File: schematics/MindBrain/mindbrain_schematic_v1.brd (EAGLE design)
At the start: 100 x 80 mm, 47 parts, among them CON1 POWER, IC1 TL084P, IC2 TL084P

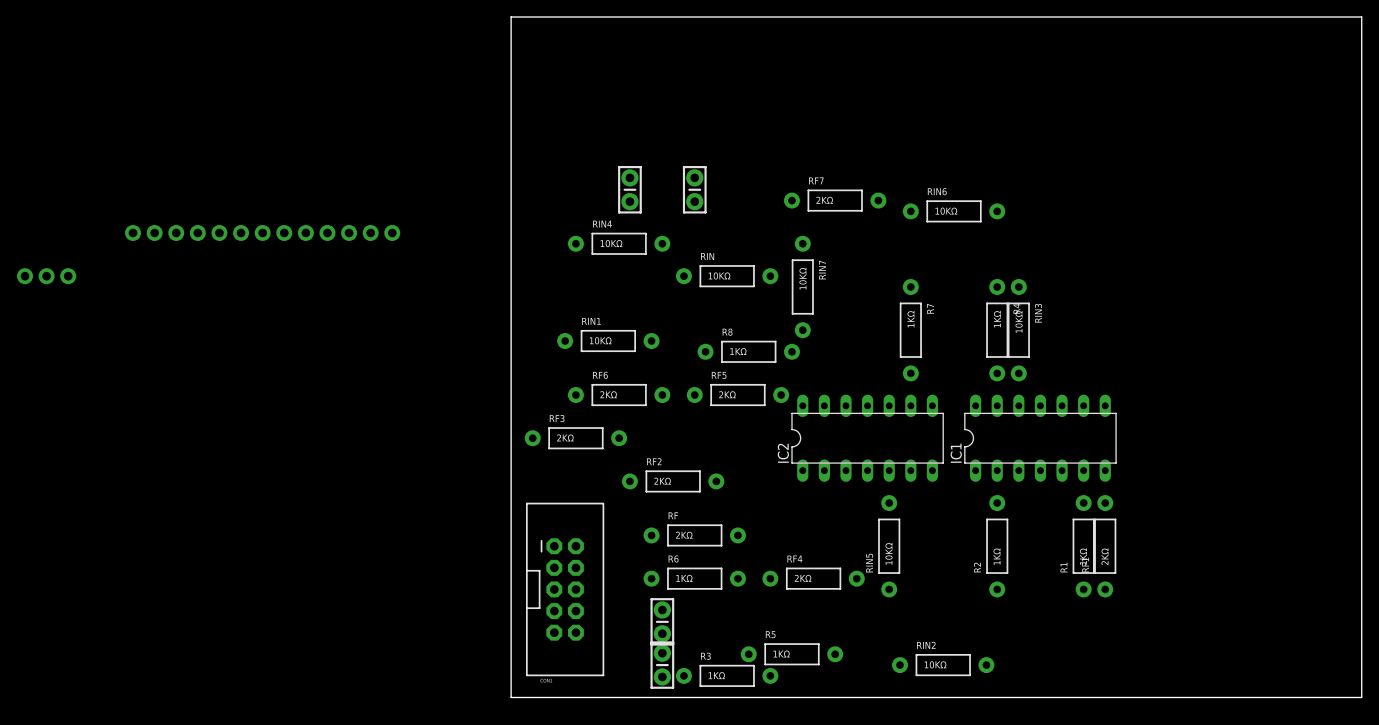
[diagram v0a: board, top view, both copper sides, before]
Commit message: fixed component designator confusion
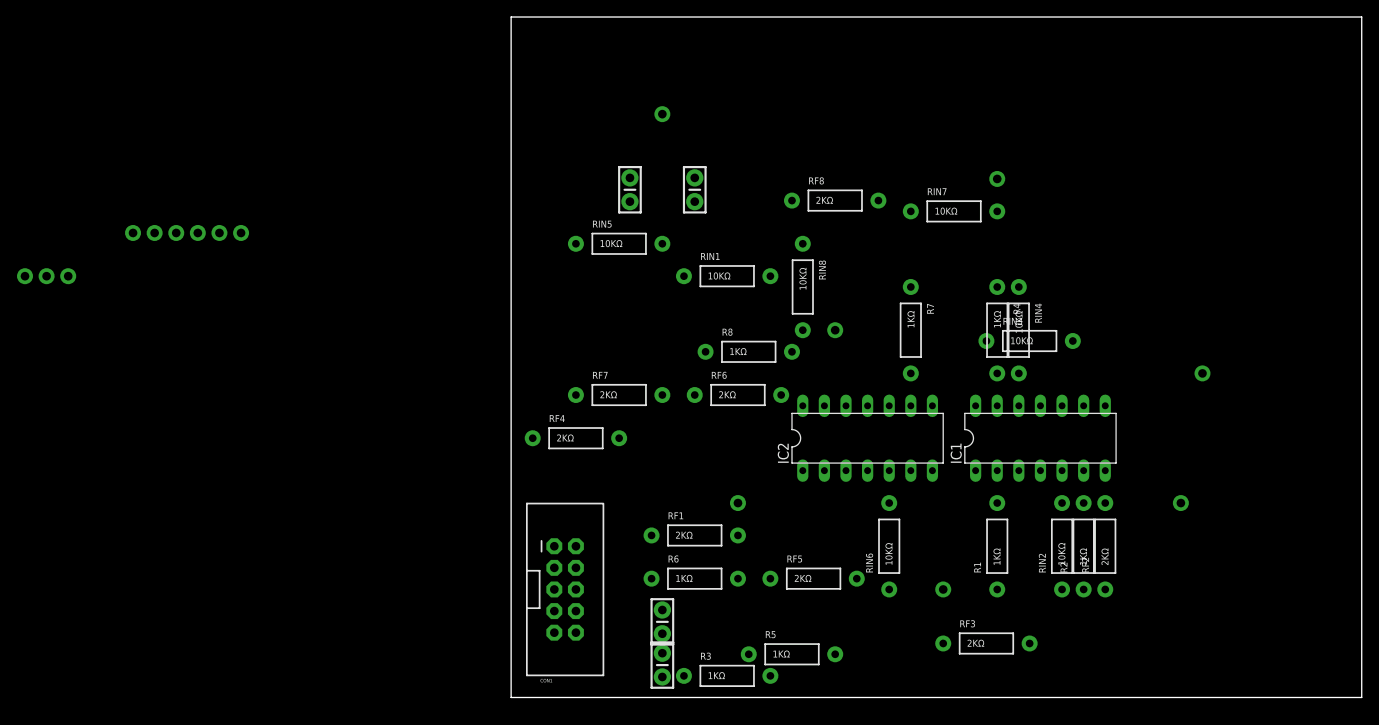
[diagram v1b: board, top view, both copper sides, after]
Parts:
- removed RF: 2KΩ, SparkFun-Passives:AXIAL-0.4
- removed RIN: 10KΩ, SparkFun-Passives:AXIAL-0.4
- added RF8: 2KΩ, SparkFun-Passives:AXIAL-0.4
- added RIN8: 10KΩ, SparkFun-Passives:AXIAL-0.4
- moved OUTPUT2 112.5 mm to (78.7, 22.9)
- moved INPUT4 96.7 mm to (81.3, 38.1)
- moved INPUT6 81.5 mm to (50.8, 12.7)
- moved INPUT7 79.0 mm to (57.1, 61.0)
- moved INPUT8 63.3 mm to (38.1, 43.2)
- moved OUTPUT1 62.1 mm to (26.7, 22.9)
- moved RF3 54.0 mm to (55.9, 6.35)
- moved RF2 51.4 mm to (69.8, 17.8), turned to 90 degrees
- moved RF1 48.3 mm to (21.6, 19.1), turned to 0 degrees
- moved RIN4 48.1 mm to (59.7, 43.2), turned to 270 degrees
- moved RIN5 47.7 mm to (12.7, 53.3), turned to 0 degrees
- moved RIN6 40.1 mm to (44.5, 17.8), turned to 90 degrees
- moved INPUT5 37.0 mm to (17.8, 68.6)
- moved RF7 34.2 mm to (12.7, 35.6)
- moved RF4 32.5 mm to (7.62, 30.5)
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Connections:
- net GND: now also RIN8.P$1; no longer RIN.P$1
- net N$1: now also RIN1.P$2; no longer RIN.P$2
- net N$10: now also RIN4.P$2; no longer RIN3.P$2
- net N$11: now also RF4.P$2; no longer RF3.P$2
- net N$12: now also RF4.P$1; no longer RF3.P$1
- net N$13: now also RIN5.P$2; no longer RIN4.P$2
- net N$14: now also RF5.P$2; no longer RF4.P$2
- net N$15: now also RF5.P$1; no longer RF4.P$1
- net N$16: now also RIN6.P$2; no longer RIN5.P$2
- net N$17: now also RF6.P$2; no longer RF5.P$2
- net N$18: now also RF6.P$1; no longer RF5.P$1
- net N$19: now also RIN7.P$2; no longer RIN6.P$2
- net N$2: now also RF1.P$2; no longer RF.P$2
- net N$20: now also RF7.P$2; no longer RF6.P$2
- net N$21: now also RF7.P$1; no longer RF6.P$1
- net N$22: now also RIN8.P$2; no longer RIN7.P$2
- net N$23: now also RF8.P$2; no longer RF7.P$2
- net N$24: now also RF8.P$1; no longer RF7.P$1
- net N$3: now also R1.P$2, RF1.P$1; no longer R2.P$2, RF.P$1
- net N$4: now also RIN2.P$2; no longer RIN1.P$2
- net N$5: now also RF2.P$2; no longer RF1.P$2
- net N$6: now also R2.P$2, RF2.P$1; no longer R1.P$2, RF1.P$1
- net N$7: now also RIN3.P$2; no longer RIN2.P$2
- net N$8: now also RF3.P$2; no longer RF2.P$2
- net N$9: now also RF3.P$1; no longer RF2.P$1

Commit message: completed basic board placement
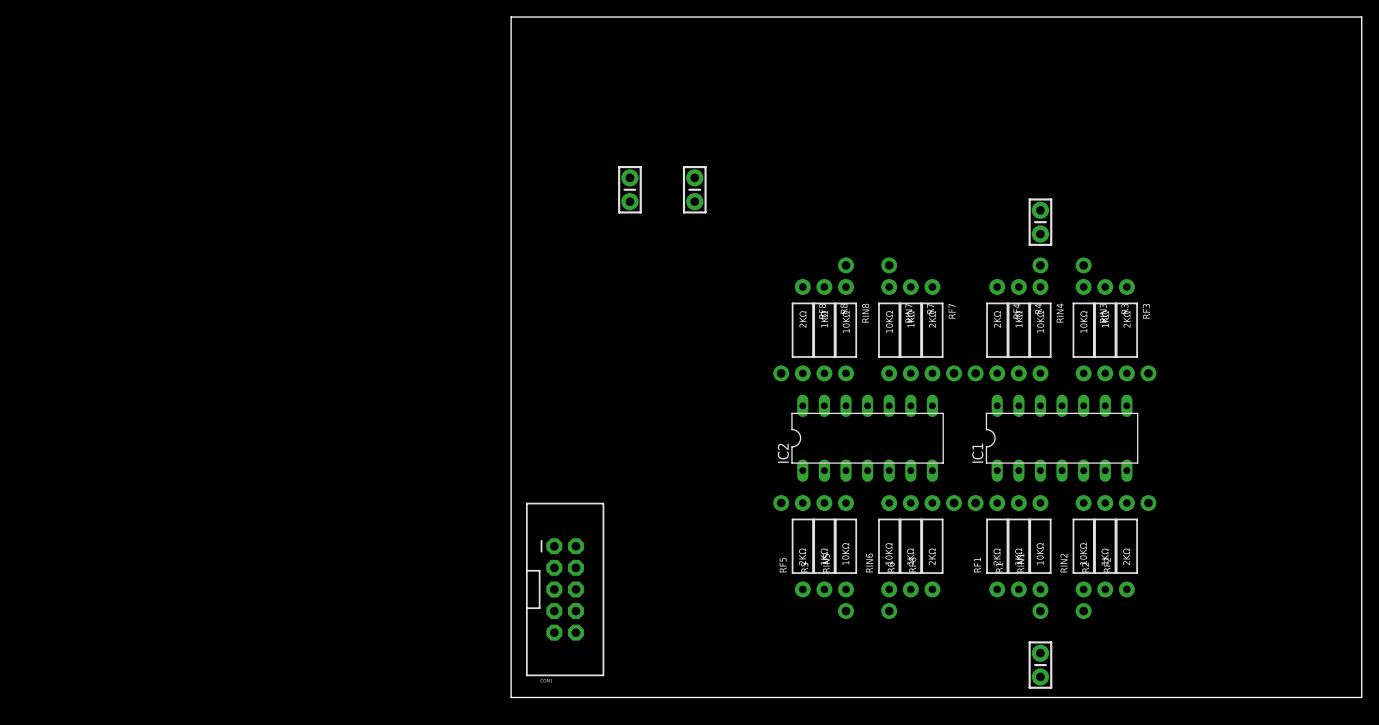
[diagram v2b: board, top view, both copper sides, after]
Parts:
- moved INPUT2 128.1 mm to (67.3, 10.2)
- moved INPUT3 124.5 mm to (67.3, 50.8)
- moved INPUT1 120.9 mm to (62.2, 10.2)
- moved OUTPUT3 108.0 mm to (74.9, 38.1)
- moved OUTPUT6 96.8 mm to (52.1, 22.9)
- moved OUTPUT7 95.4 mm to (52.1, 38.1)
- moved OUTPUT4 90.4 mm to (54.6, 38.1)
- moved OUTPUT8 78.0 mm to (31.8, 38.1)
- moved OUTPUT5 75.6 mm to (31.8, 22.9)
- moved C3 68.5 mm to (62.2, 55.9)
- moved INPUT5 62.3 mm to (39.4, 10.2)
- moved R3 60.2 mm to (69.8, 43.2), turned to 270 degrees
- moved RF4 51.1 mm to (57.1, 43.2), turned to 270 degrees
- moved RIN1 48.6 mm to (62.2, 17.8), turned to 90 degrees
- moved C2 44.7 mm to (62.2, 3.81)
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
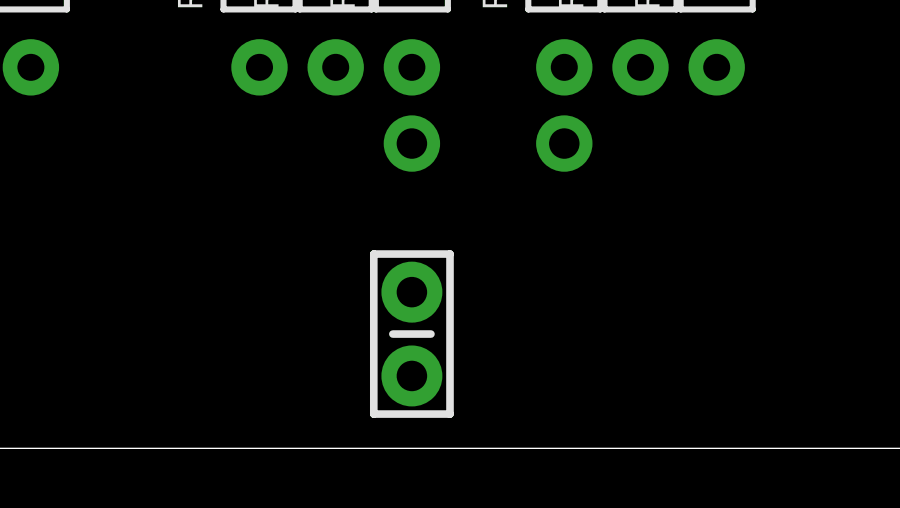
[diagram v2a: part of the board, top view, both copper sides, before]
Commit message: connected power supply grounds to circuit ground
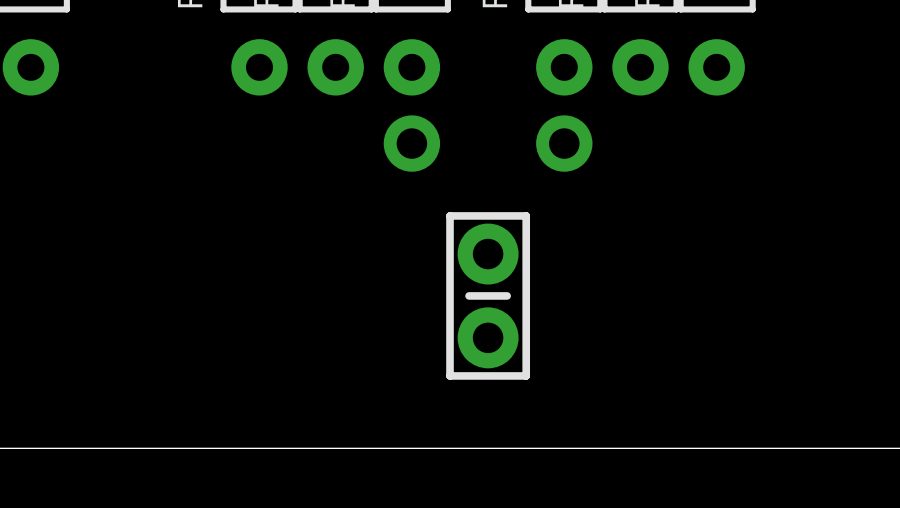
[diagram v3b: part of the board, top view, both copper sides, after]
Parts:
- moved C2 2.84 mm to (64.8, 5.08)
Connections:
- removed net N$25: CON1.3, CON1.4, CON1.5, CON1.6, CON1.7, CON1.8
- net GND: now also CON1.3, CON1.4, CON1.5, CON1.6, CON1.7, CON1.8
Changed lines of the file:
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@@
 <element name="RIN8" library="SparkFun-Passives" package="AXIAL-0.4" value="10KΩ" x="39.37" y="43.18" rot="R270"/>
 <element name="C1" library="SparkFun-Capacitors" package="CAP-PTH-SMALL-KIT" value="" x="13.97" y="59.69" rot="R90"/>
-<element name="C2" library="SparkFun-Capacitors" package="CAP-PTH-SMALL-KIT" value="" x="62.23" y="3.81" rot="R90"/>
+<element name="C2" library="SparkFun-Capacitors" package="CAP-PTH-SMALL-KIT" value="" x="64.77" y="5.08" rot="R90"/>
 <element name="C3" library="SparkFun-Capacitors" package="CAP-PTH-SMALL-KIT" value="" x="62.23" y="55.88" rot="R90"/>
 <element name="C4" library="SparkFun-Capacitors" package="CAP-PTH-SMALL-KIT" value="" x="21.59" y="59.69" rot="R90"/>
@@
 <contactref element="RIN8" pad="P$1"/>
 <contactref element="R8" pad="P$1"/>
-<wire x1="46.99" y1="12.7" x2="69.85" y2="48.26" width="0" layer="19" extent="1-1"/>
-<wire x1="59.69" y1="12.7" x2="69.85" y2="48.26" width="0" layer="19" extent="1-1"/>
-<wire x1="36.83" y1="12.7" x2="59.69" y2="12.7" width="0" layer="19" extent="1-1"/>
-<wire x1="36.83" y1="48.26" x2="36.83" y2="12.7" width="0" layer="19" extent="1-1"/>
-<wire x1="69.85" y1="12.7" x2="59.69" y2="12.7" width="0" layer="19" extent="1-1"/>
-<wire x1="59.69" y1="48.26" x2="69.85" y2="12.7" width="0" layer="19" extent="1-1"/>
+<contactref element="CON1" pad="6"/>
+<contactref element="CON1" pad="4"/>
+<contactref element="CON1" pad="8"/>
+<contactref element="CON1" pad="7"/>
+<contactref element="CON1" pad="3"/>
+<contactref element="CON1" pad="5"/>
+<wire x1="67.31" y1="48.26" x2="69.85" y2="48.26" width="0" layer="19" extent="1-1"/>
+<wire x1="62.23" y1="48.26" x2="67.31" y2="48.26" width="0" layer="19" extent="1-1"/>
+<wire x1="59.69" y1="48.26" x2="62.23" y2="48.26" width="0" layer="19" extent="1-1"/>
 <wire x1="46.99" y1="48.26" x2="59.69" y2="48.26" width="0" layer="19" extent="1-1"/>
-<wire x1="62.23" y1="12.7" x2="36.83" y2="48.26" width="0" layer="19" extent="1-1"/>
-<wire x1="62.23" y1="48.26" x2="62.23" y2="12.7" width="0" layer="19" extent="1-1"/>
-<wire x1="44.45" y1="48.26" x2="62.23" y2="48.26" width="0" layer="19" extent="1-1"/>
-<wire x1="44.45" y1="12.7" x2="44.45" y2="48.26" width="0" layer="19" extent="1-1"/>
-<wire x1="67.31" y1="48.26" x2="44.45" y2="12.7" width="0" layer="19" extent="1-1"/>
-<wire x1="67.31" y1="12.7" x2="62.23" y2="12.7" width="0" layer="19" extent="1-1"/>
-<wire x1="39.37" y1="12.7" x2="67.31" y2="12.7" width="0" layer="19" extent="1-1"/>
-<wire x1="39.37" y1="48.26" x2="39.37" y2="12.7" width="0" layer="19" extent="1-1"/>
+<wire x1="44.45" y1="48.26" x2="46.99" y2="48.26" width="0" layer="19" extent="1-1"/>
+<wire x1="39.37" y1="48.26" x2="44.45" y2="48.26" width="0" layer="19" extent="1-1"/>
+<wire x1="36.83" y1="48.26" x2="39.37" y2="48.26" width="0" layer="19" extent="1-1"/>
+<wire x1="69.85" y1="12.7" x2="69.85" y2="48.26" width="0" layer="19" extent="1-1"/>
+<wire x1="67.31" y1="12.7" x2="69.85" y2="12.7" width="0" layer="19" extent="1-1"/>
+<wire x1="62.23" y1="12.7" x2="67.31" y2="12.7" width="0" layer="19" extent="1-1"/>
+<wire x1="59.69" y1="12.7" x2="62.23" y2="12.7" width="0" layer="19" extent="1-1"/>
+<wire x1="46.99" y1="12.7" x2="59.69" y2="12.7" width="0" layer="19" extent="1-1"/>
+<wire x1="44.45" y1="12.7" x2="46.99" y2="12.7" width="0" layer="19" extent="1-1"/>
+<wire x1="39.37" y1="12.7" x2="44.45" y2="12.7" width="0" layer="19" extent="1-1"/>
+<wire x1="36.83" y1="12.7" x2="39.37" y2="12.7" width="0" layer="19" extent="1-1"/>
+<wire x1="7.62" y1="12.7" x2="36.83" y2="12.7" width="0" layer="19" extent="1-1"/>
+<wire x1="7.62" y1="15.24" x2="7.62" y2="12.7" width="0" layer="19" extent="1-1"/>
+<wire x1="5.08" y1="15.24" x2="7.62" y2="15.24" width="0" layer="19" extent="1-1"/>
+<wire x1="7.62" y1="10.16" x2="7.62" y2="12.7" width="0" layer="19" extent="1-1"/>
+<wire x1="5.08" y1="12.7" x2="7.62" y2="12.7" width="0" layer="19" extent="1-1"/>
+<wire x1="5.08" y1="10.16" x2="7.62" y2="10.16" width="0" layer="19" extent="1-1"/>
 </signal>
 <signal name="N$2">
@@
 <wire x1="34.29" y1="48.26" x2="36.83" y2="38.1" width="0" layer="19" extent="1-1"/>
 </signal>
-<signal name="N$25">
-<contactref element="CON1" pad="3"/>
-<contactref element="CON1" pad="5"/>
-<contactref element="CON1" pad="7"/>
-<contactref element="CON1" pad="6"/>
-<contactref element="CON1" pad="8"/>
-<contactref element="CON1" pad="4"/>
-<wire x1="5.08" y1="15.24" x2="7.62" y2="15.24" width="0" layer="19" extent="1-1"/>
-<wire x1="7.62" y1="12.7" x2="7.62" y2="15.24" width="0" layer="19" extent="1-1"/>
-<wire x1="5.08" y1="12.7" x2="5.08" y2="15.24" width="0" layer="19" extent="1-1"/>
-<wire x1="7.62" y1="10.16" x2="7.62" y2="12.7" width="0" layer="19" extent="1-1"/>
-<wire x1="5.08" y1="10.16" x2="5.08" y2="12.7" width="0" layer="19" extent="1-1"/>
-</signal>
 <signal name="N$27">

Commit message: made connections to bypass caps in schematic view
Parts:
- C1, C2, C3, C4: value (none) -> 0.1uF
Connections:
- removed net N$28: CON1.10, CON1.9
- removed net V+: IC1.4, IC2.4
- removed net V-: IC1.11, IC2.11
- new net N$25: C1.1, C3.1, CON1.10, CON1.9, IC1.4, IC2.4
- net GND: now also C1.2, C2.2, C3.2, C4.2
- net N$27: now also C2.1, C4.1, IC1.11, IC2.11
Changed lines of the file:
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@@
 <element name="RIN7" library="SparkFun-Passives" package="AXIAL-0.4" value="10KΩ" x="44.45" y="43.18" rot="R270"/>
 <element name="RIN8" library="SparkFun-Passives" package="AXIAL-0.4" value="10KΩ" x="39.37" y="43.18" rot="R270"/>
-<element name="C1" library="SparkFun-Capacitors" package="CAP-PTH-SMALL-KIT" value="" x="13.97" y="59.69" rot="R90"/>
-<element name="C2" library="SparkFun-Capacitors" package="CAP-PTH-SMALL-KIT" value="" x="64.77" y="5.08" rot="R90"/>
-<element name="C3" library="SparkFun-Capacitors" package="CAP-PTH-SMALL-KIT" value="" x="62.23" y="55.88" rot="R90"/>
-<element name="C4" library="SparkFun-Capacitors" package="CAP-PTH-SMALL-KIT" value="" x="21.59" y="59.69" rot="R90"/>
+<element name="C1" library="SparkFun-Capacitors" package="CAP-PTH-SMALL-KIT" value="0.1uF" x="13.97" y="59.69" rot="R90"/>
+<element name="C2" library="SparkFun-Capacitors" package="CAP-PTH-SMALL-KIT" value="0.1uF" x="64.77" y="5.08" rot="R90"/>
+<element name="C3" library="SparkFun-Capacitors" package="CAP-PTH-SMALL-KIT" value="0.1uF" x="62.23" y="55.88" rot="R90"/>
+<element name="C4" library="SparkFun-Capacitors" package="CAP-PTH-SMALL-KIT" value="0.1uF" x="21.59" y="59.69" rot="R90"/>
 <element name="CON1" library="SparkFun-Connectors" package="2X5-SHROUDED" value="POWER" x="6.35" y="12.7"/>
 </elements>
 <signals>
-<signal name="V+">
-<contactref element="IC1" pad="4"/>
-<contactref element="IC2" pad="4"/>
-<wire x1="64.77" y1="26.67" x2="41.91" y2="26.67" width="0" layer="19" extent="1-1"/>
-</signal>
-<signal name="V-">
-<contactref element="IC1" pad="11"/>
-<contactref element="IC2" pad="11"/>
-<wire x1="64.77" y1="34.29" x2="41.91" y2="34.29" width="0" layer="19" extent="1-1"/>
-</signal>
 <signal name="N$1">
 <contactref element="INPUT1" pad="1"/>
@@
 <contactref element="CON1" pad="3"/>
 <contactref element="CON1" pad="5"/>
+<contactref element="C2" pad="2"/>
+<contactref element="C4" pad="2"/>
+<contactref element="C1" pad="2"/>
+<contactref element="C3" pad="2"/>
 <wire x1="67.31" y1="48.26" x2="69.85" y2="48.26" width="0" layer="19" extent="1-1"/>
 <wire x1="62.23" y1="48.26" x2="67.31" y2="48.26" width="0" layer="19" extent="1-1"/>
 <wire x1="59.69" y1="48.26" x2="62.23" y2="48.26" width="0" layer="19" extent="1-1"/>
+<wire x1="62.23" y1="57.277" x2="62.23" y2="48.26" width="0" layer="19" extent="1-1"/>
 <wire x1="46.99" y1="48.26" x2="59.69" y2="48.26" width="0" layer="19" extent="1-1"/>
 <wire x1="44.45" y1="48.26" x2="46.99" y2="48.26" width="0" layer="19" extent="1-1"/>
 <wire x1="39.37" y1="48.26" x2="44.45" y2="48.26" width="0" layer="19" extent="1-1"/>
 <wire x1="36.83" y1="48.26" x2="39.37" y2="48.26" width="0" layer="19" extent="1-1"/>
+<wire x1="21.59" y1="61.087" x2="36.83" y2="48.26" width="0" layer="19" extent="1-1"/>
+<wire x1="13.97" y1="61.087" x2="21.59" y2="61.087" width="0" layer="19" extent="1-1"/>
 <wire x1="69.85" y1="12.7" x2="69.85" y2="48.26" width="0" layer="19" extent="1-1"/>
 <wire x1="67.31" y1="12.7" x2="69.85" y2="12.7" width="0" layer="19" extent="1-1"/>
 <wire x1="62.23" y1="12.7" x2="67.31" y2="12.7" width="0" layer="19" extent="1-1"/>
 <wire x1="59.69" y1="12.7" x2="62.23" y2="12.7" width="0" layer="19" extent="1-1"/>
+<wire x1="64.77" y1="6.477" x2="67.31" y2="12.7" width="0" layer="19" extent="1-1"/>
 <wire x1="46.99" y1="12.7" x2="59.69" y2="12.7" width="0" layer="19" extent="1-1"/>
 <wire x1="44.45" y1="12.7" x2="46.99" y2="12.7" width="0" layer="19" extent="1-1"/>
@@
 <contactref element="CON1" pad="1"/>
 <contactref element="CON1" pad="2"/>
+<contactref element="IC1" pad="11"/>
+<contactref element="IC2" pad="11"/>
+<contactref element="C2" pad="1"/>
+<contactref element="C4" pad="1"/>
+<wire x1="41.91" y1="34.29" x2="64.77" y2="34.29" width="0" layer="19" extent="1-1"/>
+<wire x1="64.77" y1="3.683" x2="64.77" y2="34.29" width="0" layer="19" extent="1-1"/>
+<wire x1="21.59" y1="58.293" x2="41.91" y2="34.29" width="0" layer="19" extent="1-1"/>
+<wire x1="7.62" y1="17.78" x2="41.91" y2="34.29" width="0" layer="19" extent="1-1"/>
 <wire x1="5.08" y1="17.78" x2="7.62" y2="17.78" width="0" layer="19" extent="1-1"/>
 </signal>
-<signal name="N$28">
+<signal name="N$25">
+<contactref element="IC1" pad="4"/>
+<contactref element="C1" pad="1"/>
 <contactref element="CON1" pad="9"/>
+<contactref element="IC2" pad="4"/>
+<contactref element="C3" pad="1"/>
 <contactref element="CON1" pad="10"/>
+<wire x1="64.77" y1="26.67" x2="62.23" y2="54.483" width="0" layer="19" extent="1-1"/>
+<wire x1="41.91" y1="26.67" x2="64.77" y2="26.67" width="0" layer="19" extent="1-1"/>
+<wire x1="7.62" y1="7.62" x2="41.91" y2="26.67" width="0" layer="19" extent="1-1"/>
 <wire x1="5.08" y1="7.62" x2="7.62" y2="7.62" width="0" layer="19" extent="1-1"/>
+<wire x1="13.97" y1="58.293" x2="41.91" y2="26.67" width="0" layer="19" extent="1-1"/>
 </signal>
 </signals>
